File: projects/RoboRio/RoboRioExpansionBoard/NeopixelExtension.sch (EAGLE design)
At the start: 5 parts, among them IC2 74HCT125N

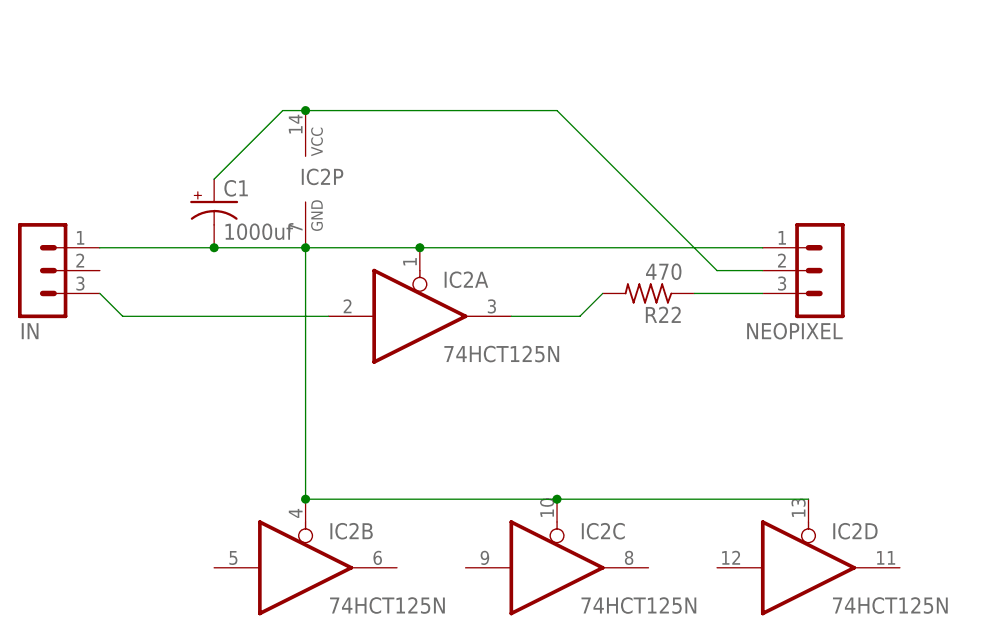
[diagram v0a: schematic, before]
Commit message: Almost finished neopixel board design
Still has slight issues with the DRC, a couple of traces go to close to
edge of board.
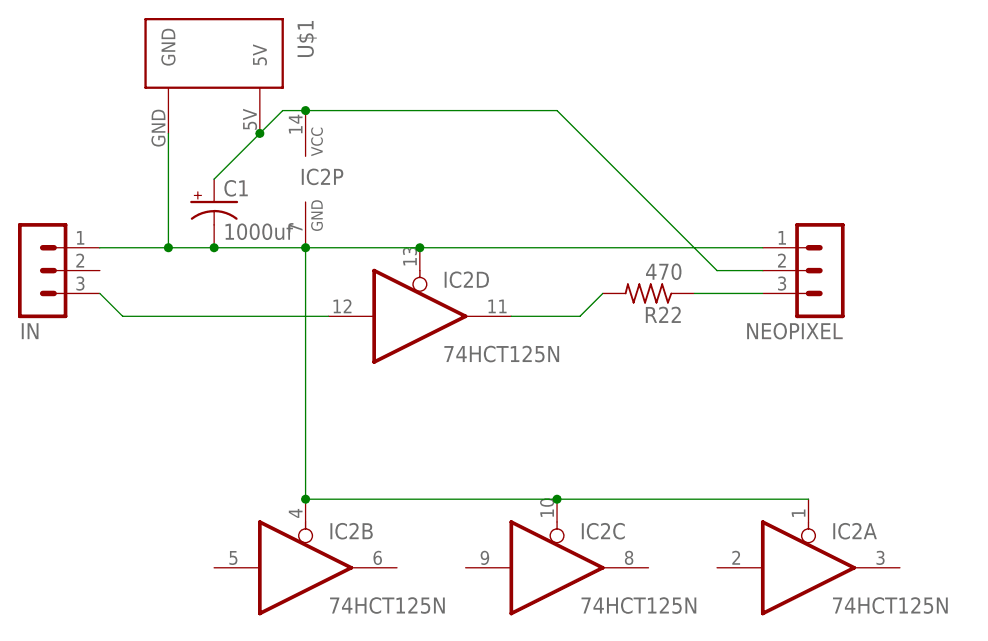
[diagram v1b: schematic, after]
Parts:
- added U$1: POWER, Molex-39543-0002:POWER
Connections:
- net GND: now also U$1.GND
- net N$3: now also IC2D.I; no longer IC2A.I
- net N$4: now also IC2D.O; no longer IC2A.O
- net VCC: now also U$1.5V
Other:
- moved on the sheet: IC2A, IC2D
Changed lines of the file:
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@@
 <part name="IN" library="con-lstb-modified" deviceset="MA03-1" device=""/>
 <part name="C1" library="adafruit" deviceset="CPOL-US" device="E5-10.5" value="1000uf"/>
+<part name="U$1" library="Molex-39543-0002" deviceset="POWER" device=""/>
 </parts>
 <sheets>
@@
 <instance part="NEOPIXEL" gate="G$1" x="109.22" y="30.48" rot="R180"/>
 <instance part="R22" gate="G$1" x="88.9" y="27.94" rot="R180"/>
-<instance part="IC2" gate="A" x="63.5" y="25.4"/>
+<instance part="IC2" gate="D" x="63.5" y="25.4"/>
 <instance part="IC2" gate="P" x="50.8" y="40.64"/>
 <instance part="IN" gate="G$1" x="20.32" y="30.48" rot="MR180"/>
 <instance part="IC2" gate="B" x="50.8" y="-2.54"/>
 <instance part="IC2" gate="C" x="78.74" y="-2.54"/>
-<instance part="IC2" gate="D" x="106.68" y="-2.54"/>
+<instance part="IC2" gate="A" x="106.68" y="-2.54"/>
 <instance part="C1" gate="G$1" x="40.64" y="38.1"/>
+<instance part="U$1" gate="G$1" x="33.02" y="50.8" rot="R270"/>
 </instances>
 <busses>
@@
 <segment>
 <pinref part="IN" gate="G$1" pin="1"/>
-<pinref part="IC2" gate="A" pin="OE"/>
-<wire x1="27.94" y1="33.02" x2="40.64" y2="33.02" width="0.1524" layer="91"/>
+<pinref part="IC2" gate="D" pin="OE"/>
+<wire x1="27.94" y1="33.02" x2="35.56" y2="33.02" width="0.1524" layer="91"/>
 <pinref part="IC2" gate="P" pin="GND"/>
+<wire x1="35.56" y1="33.02" x2="40.64" y2="33.02" width="0.1524" layer="91"/>
 <wire x1="40.64" y1="33.02" x2="50.8" y2="33.02" width="0.1524" layer="91"/>
 <wire x1="50.8" y1="33.02" x2="63.5" y2="33.02" width="0.1524" layer="91"/>
@@
 <pinref part="IC2" gate="C" pin="OE"/>
 <wire x1="50.8" y1="5.08" x2="78.74" y2="5.08" width="0.1524" layer="91"/>
-<pinref part="IC2" gate="D" pin="OE"/>
+<pinref part="IC2" gate="A" pin="OE"/>
 <wire x1="78.74" y1="5.08" x2="106.68" y2="5.08" width="0.1524" layer="91"/>
 <junction x="50.8" y="5.08"/>
@@
 <pinref part="C1" gate="G$1" pin="-"/>
 <junction x="40.64" y="33.02"/>
+<pinref part="U$1" gate="G$1" pin="GND"/>
+<wire x1="35.56" y1="45.72" x2="35.56" y2="33.02" width="0.1524" layer="91"/>
+<junction x="35.56" y="33.02"/>
 </segment>
 </net>
 <net name="N$3" class="0">
 <segment>
-<pinref part="IC2" gate="A" pin="I"/>
+<pinref part="IC2" gate="D" pin="I"/>
 <pinref part="IN" gate="G$1" pin="3"/>
 <wire x1="53.34" y1="25.4" x2="30.48" y2="25.4" width="0.1524" layer="91"/>
@@
 <net name="N$4" class="0">
 <segment>
-<pinref part="IC2" gate="A" pin="O"/>
+<pinref part="IC2" gate="D" pin="O"/>
 <pinref part="R22" gate="G$1" pin="2"/>
 <wire x1="73.66" y1="25.4" x2="81.28" y2="25.4" width="0.1524" layer="91"/>
@@
 <wire x1="101.6" y1="30.48" x2="96.52" y2="30.48" width="0.1524" layer="91"/>
 <pinref part="IC2" gate="P" pin="VCC"/>
-<wire x1="40.64" y1="40.64" x2="48.26" y2="48.26" width="0.1524" layer="91"/>
+<wire x1="40.64" y1="40.64" x2="45.72" y2="45.72" width="0.1524" layer="91"/>
+<wire x1="45.72" y1="45.72" x2="48.26" y2="48.26" width="0.1524" layer="91"/>
 <wire x1="48.26" y1="48.26" x2="50.8" y2="48.26" width="0.1524" layer="91"/>
 <wire x1="96.52" y1="30.48" x2="78.74" y2="48.26" width="0.1524" layer="91"/>
@@
 <junction x="50.8" y="48.26"/>
 <pinref part="C1" gate="G$1" pin="+"/>
+<pinref part="U$1" gate="G$1" pin="5V"/>
+<junction x="45.72" y="45.72"/>
 </segment>
 </net>

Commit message: Finished neopixel extension schematic and layout.
Still need to double-check neopixel connector and DRC.
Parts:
- removed NEOPIXEL: (no value), con-lstb-modified:MA03-1
- added U$2: NEOPIXEL1, NeopixelConnector:NEOPIXEL1
- renumbered R22 to R1
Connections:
- net GND: now also U$2.GND; no longer NEOPIXEL.1
- net N$1: now also U$2.SIGNAL; no longer NEOPIXEL.3
- net VCC: now also U$2.VCC; no longer NEOPIXEL.2
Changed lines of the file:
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@@
 </classes>
 <parts>
-<part name="NEOPIXEL" library="con-lstb-modified" deviceset="MA03-1" device=""/>
-<part name="R22" library="resistor" deviceset="R-US_" device="0309/V" value="470"/>
+<part name="R1" library="resistor" deviceset="R-US_" device="0309/V" value="470"/>
 <part name="IC2" library="74xx-eu" deviceset="74*125" device="N" technology="HCT"/>
 <part name="IN" library="con-lstb-modified" deviceset="MA03-1" device=""/>
 <part name="C1" library="adafruit" deviceset="CPOL-US" device="E5-10.5" value="1000uf"/>
 <part name="U$1" library="Molex-39543-0002" deviceset="POWER" device=""/>
+<part name="U$2" library="NeopixelConnector" deviceset="NEOPIXEL1" device=""/>
 </parts>
 <sheets>
@@
 </plain>
 <instances>
-<instance part="NEOPIXEL" gate="G$1" x="109.22" y="30.48" rot="R180"/>
-<instance part="R22" gate="G$1" x="88.9" y="27.94" rot="R180"/>
+<instance part="R1" gate="G$1" x="88.9" y="27.94" rot="R180"/>
 <instance part="IC2" gate="D" x="63.5" y="25.4"/>
 <instance part="IC2" gate="P" x="50.8" y="40.64"/>
@@
 <instance part="C1" gate="G$1" x="40.64" y="38.1"/>
 <instance part="U$1" gate="G$1" x="33.02" y="50.8" rot="R270"/>
+<instance part="U$2" gate="G$1" x="106.68" y="30.48" rot="MR180"/>
 </instances>
 <busses>
@@
 <net name="N$1" class="0">
 <segment>
-<pinref part="NEOPIXEL" gate="G$1" pin="3"/>
-<pinref part="R22" gate="G$1" pin="1"/>
-<wire x1="93.98" y1="27.94" x2="101.6" y2="27.94" width="0.1524" layer="91"/>
+<pinref part="R1" gate="G$1" pin="1"/>
+<pinref part="U$2" gate="G$1" pin="SIGNAL"/>
+<wire x1="101.6" y1="27.94" x2="93.98" y2="27.94" width="0.1524" layer="91"/>
 </segment>
 </net>
@@
 <wire x1="50.8" y1="33.02" x2="63.5" y2="33.02" width="0.1524" layer="91"/>
 <junction x="50.8" y="33.02"/>
-<pinref part="NEOPIXEL" gate="G$1" pin="1"/>
-<wire x1="63.5" y1="33.02" x2="101.6" y2="33.02" width="0.1524" layer="91"/>
-<junction x="63.5" y="33.02"/>
 <wire x1="50.8" y1="33.02" x2="50.8" y2="5.08" width="0.1524" layer="91"/>
 <pinref part="IC2" gate="B" pin="OE"/>
@@
 <wire x1="35.56" y1="45.72" x2="35.56" y2="33.02" width="0.1524" layer="91"/>
 <junction x="35.56" y="33.02"/>
+<pinref part="U$2" gate="G$1" pin="GND"/>
+<wire x1="101.6" y1="33.02" x2="63.5" y2="33.02" width="0.1524" layer="91"/>
+<junction x="63.5" y="33.02"/>
 </segment>
 </net>
@@
 <segment>
 <pinref part="IC2" gate="D" pin="O"/>
-<pinref part="R22" gate="G$1" pin="2"/>
+<pinref part="R1" gate="G$1" pin="2"/>
 <wire x1="73.66" y1="25.4" x2="81.28" y2="25.4" width="0.1524" layer="91"/>
 <wire x1="81.28" y1="25.4" x2="83.82" y2="27.94" width="0.1524" layer="91"/>
@@
 <net name="VCC" class="0">
 <segment>
-<pinref part="NEOPIXEL" gate="G$1" pin="2"/>
-<wire x1="101.6" y1="30.48" x2="96.52" y2="30.48" width="0.1524" layer="91"/>
 <pinref part="IC2" gate="P" pin="VCC"/>
 <wire x1="40.64" y1="40.64" x2="45.72" y2="45.72" width="0.1524" layer="91"/>
 <wire x1="45.72" y1="45.72" x2="48.26" y2="48.26" width="0.1524" layer="91"/>
 <wire x1="48.26" y1="48.26" x2="50.8" y2="48.26" width="0.1524" layer="91"/>
-<wire x1="96.52" y1="30.48" x2="78.74" y2="48.26" width="0.1524" layer="91"/>
 <wire x1="78.74" y1="48.26" x2="50.8" y2="48.26" width="0.1524" layer="91"/>
 <junction x="50.8" y="48.26"/>
@@
 <pinref part="U$1" gate="G$1" pin="5V"/>
 <junction x="45.72" y="45.72"/>
+<pinref part="U$2" gate="G$1" pin="VCC"/>
+<wire x1="101.6" y1="30.48" x2="96.52" y2="30.48" width="0.1524" layer="91"/>
+<wire x1="96.52" y1="30.48" x2="78.74" y2="48.26" width="0.1524" layer="91"/>
 </segment>
 </net>

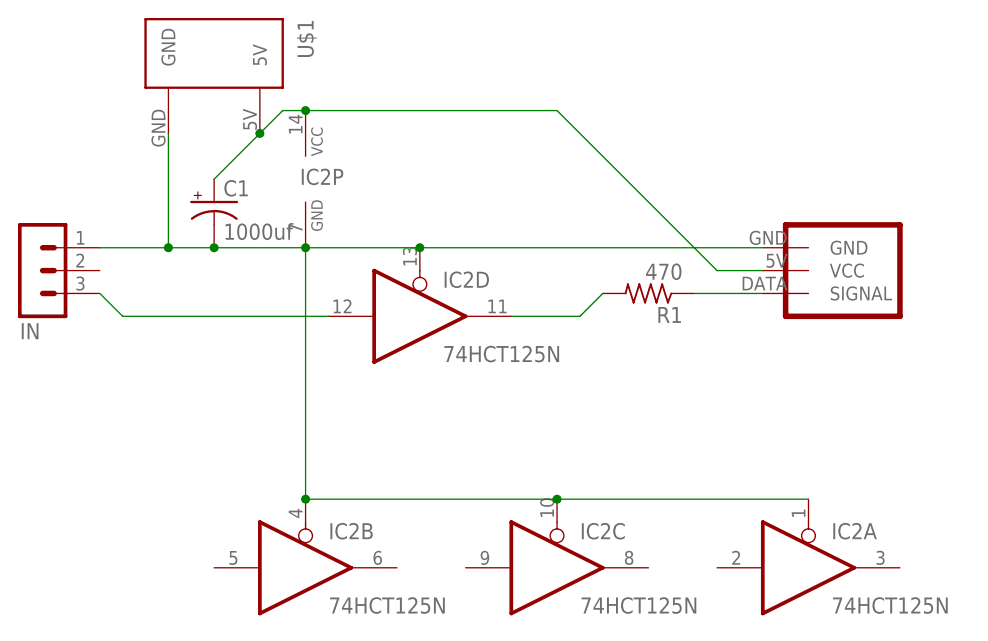
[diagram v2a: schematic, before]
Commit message: Updated neopixel connector
to use AND gate for level shifter
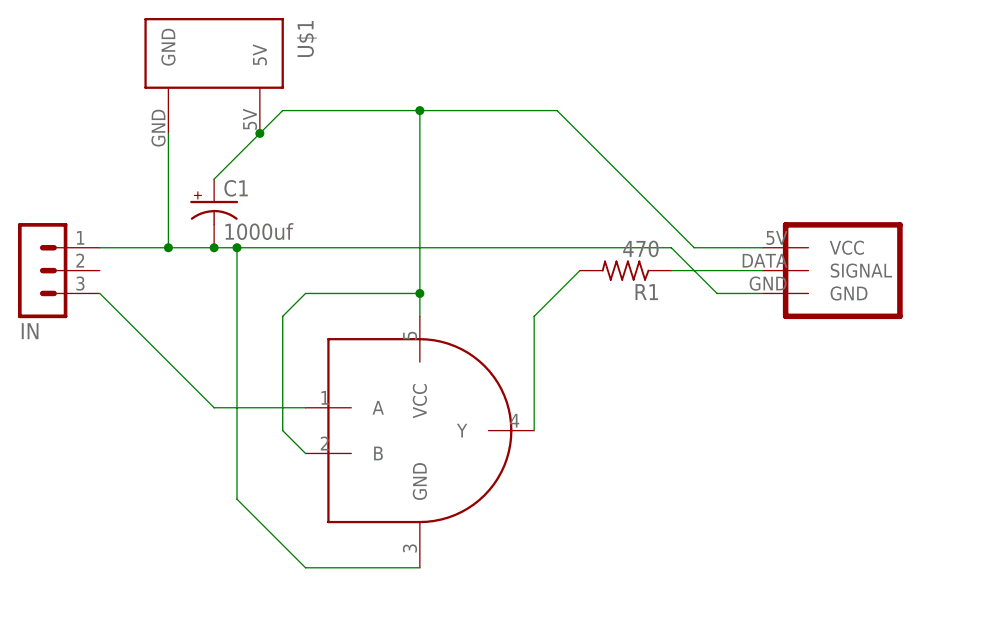
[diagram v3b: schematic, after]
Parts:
- removed IC2: 74HCT125N, 74xx-eu:74HCT125N
- added U$3: 74AHCT1G08, SOT25:74AHCT1G08
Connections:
- net GND: now also U$3.GND; no longer IC2A.OE, IC2B.OE, IC2C.OE, IC2D.OE, IC2P.GND
- net N$3: no longer IC2D.I
- net N$4: now also U$3.Y; no longer IC2D.O
- net VCC: now also U$3.B, U$3.VCC; no longer IC2P.VCC
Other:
- moved on the sheet: R1
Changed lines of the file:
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@@
 <parts>
 <part name="R1" library="resistor" deviceset="R-US_" device="0309/V" value="470"/>
-<part name="IC2" library="74xx-eu" deviceset="74*125" device="N" technology="HCT"/>
 <part name="IN" library="con-lstb-modified" deviceset="MA03-1" device=""/>
 <part name="C1" library="adafruit" deviceset="CPOL-US" device="E5-10.5" value="1000uf"/>
 <part name="U$1" library="Molex-39543-0002" deviceset="POWER" device=""/>
 <part name="U$2" library="NeopixelConnector" deviceset="NEOPIXEL1" device=""/>
+<part name="U$3" library="SOT25" deviceset="74AHCT1G08" device=""/>
 </parts>
 <sheets>
@@
 </plain>
 <instances>
-<instance part="R1" gate="G$1" x="88.9" y="27.94" rot="R180"/>
-<instance part="IC2" gate="D" x="63.5" y="25.4"/>
-<instance part="IC2" gate="P" x="50.8" y="40.64"/>
+<instance part="R1" gate="G$1" x="86.36" y="30.48" rot="R180"/>
 <instance part="IN" gate="G$1" x="20.32" y="30.48" rot="MR180"/>
-<instance part="IC2" gate="B" x="50.8" y="-2.54"/>
-<instance part="IC2" gate="C" x="78.74" y="-2.54"/>
-<instance part="IC2" gate="A" x="106.68" y="-2.54"/>
 <instance part="C1" gate="G$1" x="40.64" y="38.1"/>
 <instance part="U$1" gate="G$1" x="33.02" y="50.8" rot="R270"/>
 <instance part="U$2" gate="G$1" x="106.68" y="30.48" rot="MR180"/>
+<instance part="U$3" gate="AND" x="66.04" y="12.7"/>
 </instances>
 <busses>
@@
 <pinref part="R1" gate="G$1" pin="1"/>
 <pinref part="U$2" gate="G$1" pin="SIGNAL"/>
-<wire x1="101.6" y1="27.94" x2="93.98" y2="27.94" width="0.1524" layer="91"/>
+<wire x1="101.6" y1="30.48" x2="91.44" y2="30.48" width="0.1524" layer="91"/>
 </segment>
 </net>
@@
 <segment>
 <pinref part="IN" gate="G$1" pin="1"/>
-<pinref part="IC2" gate="D" pin="OE"/>
 <wire x1="27.94" y1="33.02" x2="35.56" y2="33.02" width="0.1524" layer="91"/>
-<pinref part="IC2" gate="P" pin="GND"/>
 <wire x1="35.56" y1="33.02" x2="40.64" y2="33.02" width="0.1524" layer="91"/>
-<wire x1="40.64" y1="33.02" x2="50.8" y2="33.02" width="0.1524" layer="91"/>
-<wire x1="50.8" y1="33.02" x2="63.5" y2="33.02" width="0.1524" layer="91"/>
-<junction x="50.8" y="33.02"/>
-<wire x1="50.8" y1="33.02" x2="50.8" y2="5.08" width="0.1524" layer="91"/>
-<pinref part="IC2" gate="B" pin="OE"/>
-<pinref part="IC2" gate="C" pin="OE"/>
-<wire x1="50.8" y1="5.08" x2="78.74" y2="5.08" width="0.1524" layer="91"/>
-<pinref part="IC2" gate="A" pin="OE"/>
-<wire x1="78.74" y1="5.08" x2="106.68" y2="5.08" width="0.1524" layer="91"/>
-<junction x="50.8" y="5.08"/>
-<junction x="78.74" y="5.08"/>
+<wire x1="40.64" y1="33.02" x2="43.18" y2="33.02" width="0.1524" layer="91"/>
 <pinref part="C1" gate="G$1" pin="-"/>
 <junction x="40.64" y="33.02"/>
@@
 <junction x="35.56" y="33.02"/>
 <pinref part="U$2" gate="G$1" pin="GND"/>
-<wire x1="101.6" y1="33.02" x2="63.5" y2="33.02" width="0.1524" layer="91"/>
-<junction x="63.5" y="33.02"/>
+<wire x1="101.6" y1="27.94" x2="96.52" y2="27.94" width="0.1524" layer="91"/>
+<wire x1="96.52" y1="27.94" x2="91.44" y2="33.02" width="0.1524" layer="91"/>
+<wire x1="91.44" y1="33.02" x2="43.18" y2="33.02" width="0.1524" layer="91"/>
+<wire x1="43.18" y1="33.02" x2="43.18" y2="5.08" width="0.1524" layer="91"/>
+<wire x1="43.18" y1="5.08" x2="50.8" y2="-2.54" width="0.1524" layer="91"/>
+<pinref part="U$3" gate="AND" pin="GND"/>
+<wire x1="50.8" y1="-2.54" x2="63.5" y2="-2.54" width="0.1524" layer="91"/>
+<junction x="43.18" y="33.02"/>
 </segment>
 </net>
 <net name="N$3" class="0">
 <segment>
-<pinref part="IC2" gate="D" pin="I"/>
 <pinref part="IN" gate="G$1" pin="3"/>
-<wire x1="53.34" y1="25.4" x2="30.48" y2="25.4" width="0.1524" layer="91"/>
-<wire x1="30.48" y1="25.4" x2="27.94" y2="27.94" width="0.1524" layer="91"/>
+<wire x1="50.8" y1="15.24" x2="40.64" y2="15.24" width="0.1524" layer="91"/>
+<wire x1="40.64" y1="15.24" x2="27.94" y2="27.94" width="0.1524" layer="91"/>
 </segment>
 </net>
 <net name="N$4" class="0">
 <segment>
-<pinref part="IC2" gate="D" pin="O"/>
 <pinref part="R1" gate="G$1" pin="2"/>
-<wire x1="73.66" y1="25.4" x2="81.28" y2="25.4" width="0.1524" layer="91"/>
-<wire x1="81.28" y1="25.4" x2="83.82" y2="27.94" width="0.1524" layer="91"/>
+<wire x1="76.2" y1="25.4" x2="81.28" y2="30.48" width="0.1524" layer="91"/>
+<pinref part="U$3" gate="AND" pin="Y"/>
+<wire x1="76.2" y1="25.4" x2="76.2" y2="12.7" width="0.1524" layer="91"/>
 </segment>
 </net>
 <net name="VCC" class="0">
 <segment>
-<pinref part="IC2" gate="P" pin="VCC"/>
 <wire x1="40.64" y1="40.64" x2="45.72" y2="45.72" width="0.1524" layer="91"/>
 <wire x1="45.72" y1="45.72" x2="48.26" y2="48.26" width="0.1524" layer="91"/>
-<wire x1="48.26" y1="48.26" x2="50.8" y2="48.26" width="0.1524" layer="91"/>
-<wire x1="78.74" y1="48.26" x2="50.8" y2="48.26" width="0.1524" layer="91"/>
-<junction x="50.8" y="48.26"/>
+<wire x1="78.74" y1="48.26" x2="63.5" y2="48.26" width="0.1524" layer="91"/>
 <pinref part="C1" gate="G$1" pin="+"/>
 <pinref part="U$1" gate="G$1" pin="5V"/>
 <junction x="45.72" y="45.72"/>
 <pinref part="U$2" gate="G$1" pin="VCC"/>
-<wire x1="101.6" y1="30.48" x2="96.52" y2="30.48" width="0.1524" layer="91"/>
-<wire x1="96.52" y1="30.48" x2="78.74" y2="48.26" width="0.1524" layer="91"/>
+<wire x1="63.5" y1="48.26" x2="48.26" y2="48.26" width="0.1524" layer="91"/>
+<wire x1="101.6" y1="33.02" x2="93.98" y2="33.02" width="0.1524" layer="91"/>
+<wire x1="93.98" y1="33.02" x2="78.74" y2="48.26" width="0.1524" layer="91"/>
+<pinref part="U$3" gate="AND" pin="VCC"/>
+<wire x1="63.5" y1="48.26" x2="63.5" y2="27.94" width="0.1524" layer="91"/>
+<junction x="63.5" y="48.26"/>
+<junction x="63.5" y="27.94"/>
+<wire x1="63.5" y1="27.94" x2="63.5" y2="25.4" width="0.1524" layer="91"/>
+<wire x1="63.5" y1="27.94" x2="50.8" y2="27.94" width="0.1524" layer="91"/>
+<wire x1="50.8" y1="27.94" x2="48.26" y2="25.4" width="0.1524" layer="91"/>
+<pinref part="U$3" gate="AND" pin="B"/>
+<wire x1="48.26" y1="25.4" x2="48.26" y2="12.7" width="0.1524" layer="91"/>
+<wire x1="48.26" y1="12.7" x2="50.8" y2="10.16" width="0.1524" layer="91"/>
 </segment>
 </net>

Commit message: Finished NeopixelRev1
We should probably publish this.
Will work on a rev2 soon
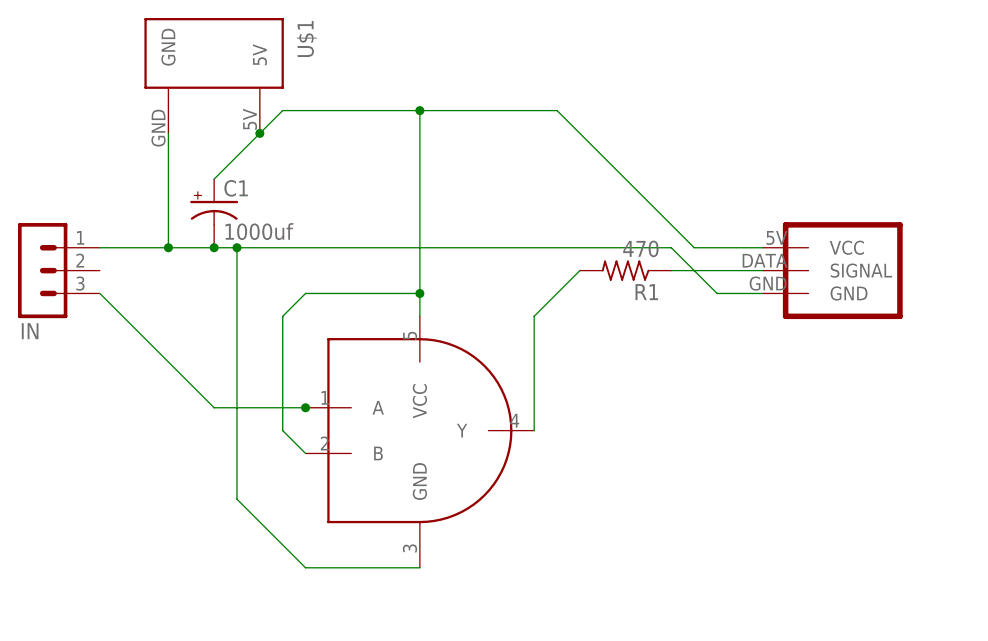
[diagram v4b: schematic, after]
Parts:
- renumbered U$3 to S1
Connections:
- net N$3: now also S1.A
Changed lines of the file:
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@@
 <part name="U$1" library="Molex-39543-0002" deviceset="POWER" device=""/>
 <part name="U$2" library="NeopixelConnector" deviceset="NEOPIXEL1" device=""/>
-<part name="U$3" library="SOT25" deviceset="74AHCT1G08" device=""/>
+<part name="S1" library="SOT25" deviceset="74AHCT1G08" device=""/>
 </parts>
 <sheets>
@@
 <instance part="U$1" gate="G$1" x="33.02" y="50.8" rot="R270"/>
 <instance part="U$2" gate="G$1" x="106.68" y="30.48" rot="MR180"/>
-<instance part="U$3" gate="AND" x="66.04" y="12.7"/>
+<instance part="S1" gate="AND" x="66.04" y="12.7"/>
 </instances>
 <busses>
@@
 <wire x1="43.18" y1="33.02" x2="43.18" y2="5.08" width="0.1524" layer="91"/>
 <wire x1="43.18" y1="5.08" x2="50.8" y2="-2.54" width="0.1524" layer="91"/>
-<pinref part="U$3" gate="AND" pin="GND"/>
+<pinref part="S1" gate="AND" pin="GND"/>
 <wire x1="50.8" y1="-2.54" x2="63.5" y2="-2.54" width="0.1524" layer="91"/>
 <junction x="43.18" y="33.02"/>
@@
 <wire x1="50.8" y1="15.24" x2="40.64" y2="15.24" width="0.1524" layer="91"/>
 <wire x1="40.64" y1="15.24" x2="27.94" y2="27.94" width="0.1524" layer="91"/>
+<pinref part="S1" gate="AND" pin="A"/>
+<junction x="50.8" y="15.24"/>
 </segment>
 </net>
@@
 <pinref part="R1" gate="G$1" pin="2"/>
 <wire x1="76.2" y1="25.4" x2="81.28" y2="30.48" width="0.1524" layer="91"/>
-<pinref part="U$3" gate="AND" pin="Y"/>
+<pinref part="S1" gate="AND" pin="Y"/>
 <wire x1="76.2" y1="25.4" x2="76.2" y2="12.7" width="0.1524" layer="91"/>
 </segment>
@@
 <wire x1="101.6" y1="33.02" x2="93.98" y2="33.02" width="0.1524" layer="91"/>
 <wire x1="93.98" y1="33.02" x2="78.74" y2="48.26" width="0.1524" layer="91"/>
-<pinref part="U$3" gate="AND" pin="VCC"/>
+<pinref part="S1" gate="AND" pin="VCC"/>
 <wire x1="63.5" y1="48.26" x2="63.5" y2="27.94" width="0.1524" layer="91"/>
 <junction x="63.5" y="48.26"/>
@@
 <wire x1="63.5" y1="27.94" x2="50.8" y2="27.94" width="0.1524" layer="91"/>
 <wire x1="50.8" y1="27.94" x2="48.26" y2="25.4" width="0.1524" layer="91"/>
-<pinref part="U$3" gate="AND" pin="B"/>
+<pinref part="S1" gate="AND" pin="B"/>
 <wire x1="48.26" y1="25.4" x2="48.26" y2="12.7" width="0.1524" layer="91"/>
 <wire x1="48.26" y1="12.7" x2="50.8" y2="10.16" width="0.1524" layer="91"/>
